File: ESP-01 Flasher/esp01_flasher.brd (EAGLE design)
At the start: 27.9 x 34 mm, 8 parts

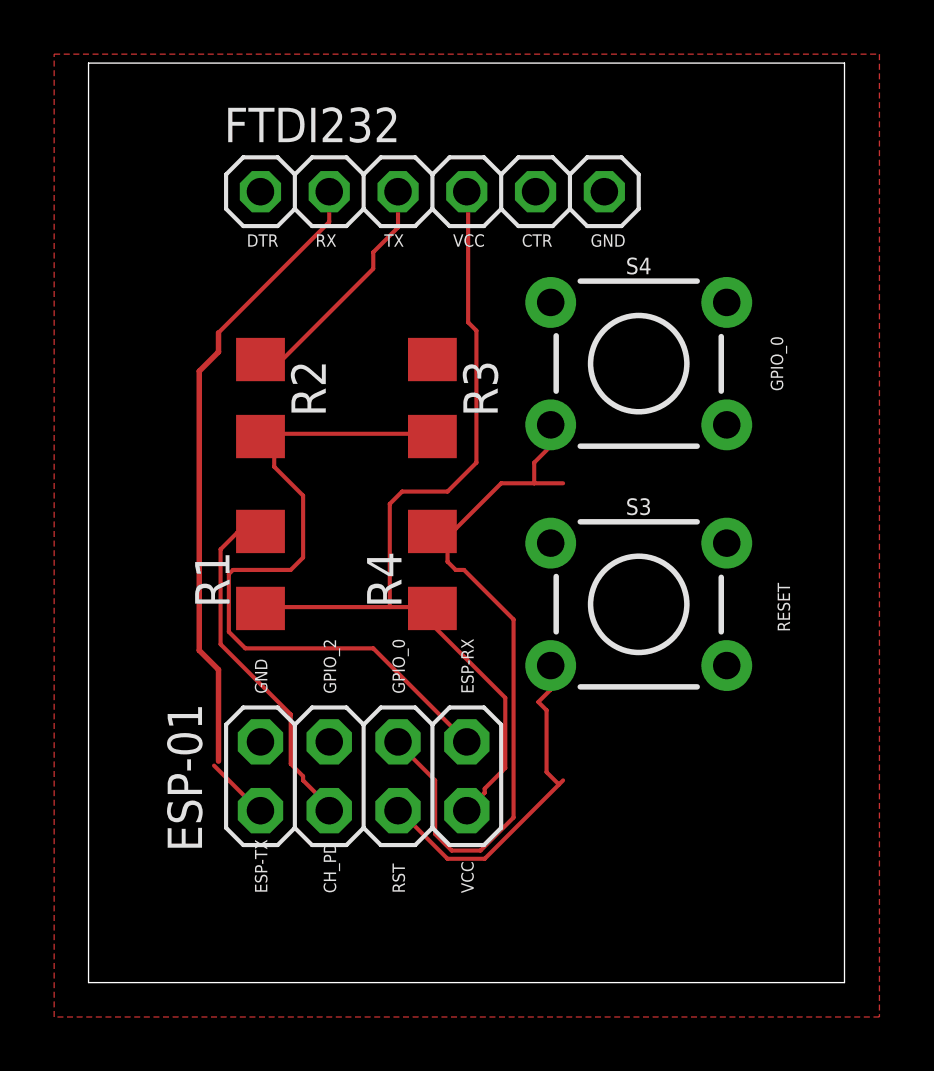
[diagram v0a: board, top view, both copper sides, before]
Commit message: ESP-01 Flasher v0.2
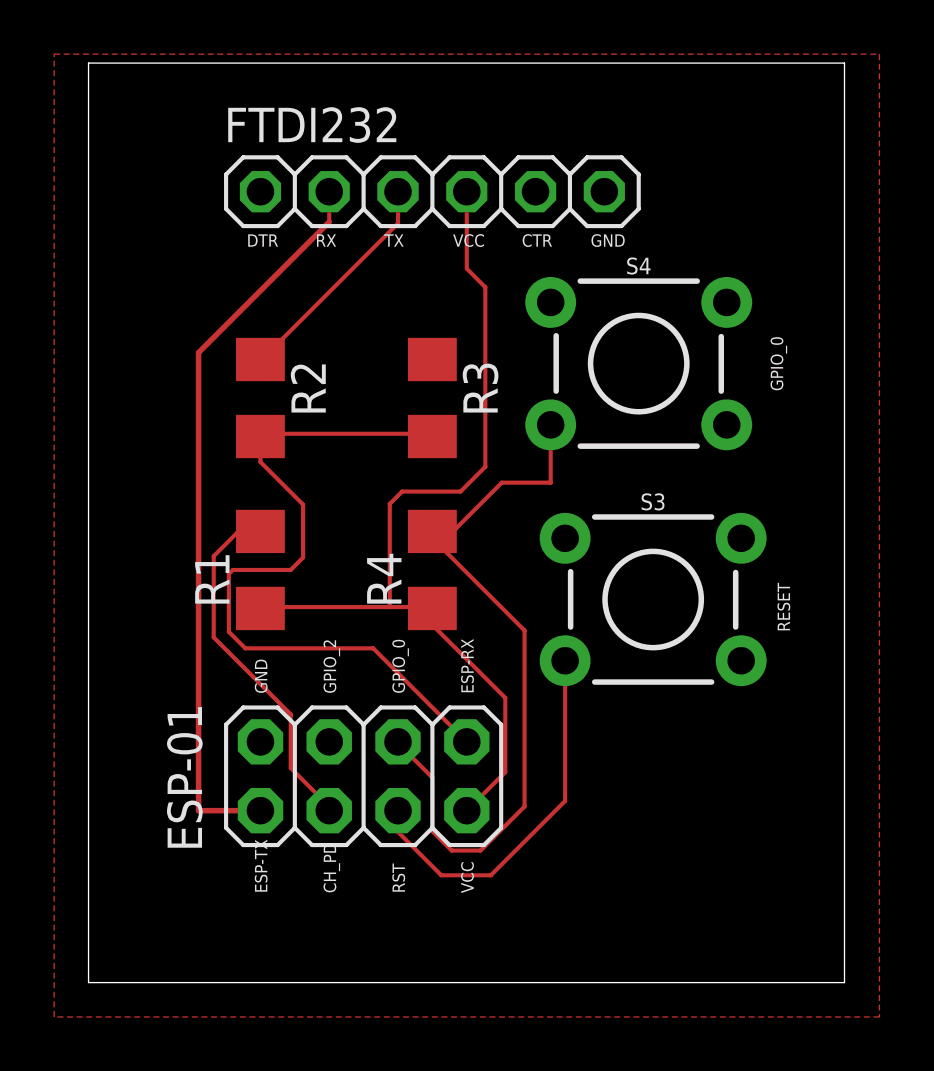
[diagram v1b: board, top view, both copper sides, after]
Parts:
- moved S3 0.56 mm to (20.9, 14.1)
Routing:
- net ESP-TX: track 25.7 -> 27.1 mm
- net RST: track 13.0 -> 13.9 mm
- net VCC: track 33.4 -> 33.9 mm
- net GPIO_0: track 28.0 -> 27.5 mm
